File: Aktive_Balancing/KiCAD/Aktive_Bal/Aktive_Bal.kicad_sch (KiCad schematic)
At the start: 167 parts, among them J1 Conn_01x01_Pin, J2 Sockel_BluePill, J3 A-DF_09_A_KG-T4S, J4 Screw_Terminal_01x02, J5 Conn_01x01_Pin, J6 Conn_01x01_Pin, Q1 BSS316NH6327XTSA1, Q10 NTTFS6H888NL, Q11 NTTFS6H888NL, Q12 NTTFS6H888NL, Q13 NTTFS6H888NL, Q14 NTTFS6H888NL, Q15 NTTFS6H888NL, Q16 NTTFS6H888NL, Q17 NTTFS6H888NL, Q18 NTTFS6H888NL, Q19 NTTFS6H888NL, Q20 NTTFS6H888NL, Q21 NTTFS6H888NL, Q22 NTTFS6H888NL, Q23 NTTFS6H888NL, Q24 NTTFS6H888NL, Q25 NTTFS6H888NL, Q26 NTTFS6H888NL, Q27 NTTFS6H888NL, Q28 NTTFS6H888NL, Q29 NTTFS6H888NL, Q3 NTTFS6H888NL, Q30 NTTFS6H888NL, Q31 NTTFS6H888NL, Q32 NTTFS6H888NL, Q33 NTTFS6H888NL, Q34 NTTFS6H888NL, Q4 NTTFS6H888NL, Q5 NTTFS6H888NL, Q6 NTTFS6H888NL, Q7 NTTFS6H888NL, Q8 NTTFS6H888NL, Q9 NTTFS6H888NL, U1 SCW20C-12, U10 LTV-847S, U11 LTV-847S, U12 LTV-847S, U13 RFP12N10L, U14 PCF8575CDB, U15 SN65HVD233, U2 EC1SA16N, U3 LM2596S-ADJ, U4 TL084, U5 ADUM1250ARZ-RL7, U6 PCA9306DC, U7 LM1117IMPX_3_3_NOPB, U8 MCP4725xxx-xCH, U9 LTV-847S

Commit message: footprints zuggewiesen
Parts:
- C1: footprint (none) -> Capacitor_SMD:C_Elec_8x10.2
- C4: footprint (none) -> Capacitor_SMD:CP_Elec_5x5.3
- D1: footprint (none) -> Diode_SMD:D_SMA
- J4: footprint (none) -> TerminalBlock_MetzConnect:TerminalBlock_MetzConnect_Type055_RT01502HDWU_1x02_P5.00mm_Horizontal
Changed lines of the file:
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@@
 			)
 		)
-		(property "Footprint" ""
+		(property "Footprint" "TerminalBlock_MetzConnect:TerminalBlock_MetzConnect_Type055_RT01502HDWU_1x02_P5.00mm_Horizontal"
 			(at 24.13 40.64 0)
 			(hide yes)
@@
 			)
 		)
-		(property "Footprint" ""
+		(property "Footprint" "Capacitor_SMD:C_Elec_8x10.2"
 			(at 166.37 205.74 0)
 			(hide yes)
@@
 			)
 		)
-		(property "Footprint" ""
+		(property "Footprint" "Diode_SMD:D_SMA"
 			(at 200.025 214.63 0)
 			(hide yes)
@@
 			)
 		)
-		(property "Footprint" ""
+		(property "Footprint" "Capacitor_SMD:CP_Elec_5x5.3"
 			(at 216.8652 218.44 0)
 			(hide yes)

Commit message: footprints
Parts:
- added J7, J8, J9: Conn_01x01_Pin, Connector_PinHeader_2.54mm:PinHeader_1x01_P2.54mm_Vertical, symbol Connector:Conn_01x01_Pin
- J1, J5, J6: footprint (none) -> Connector_PinHeader_2.54mm:PinHeader_1x01_P2.54mm_Vertical
- JP1: footprint (none) -> Jumper:SolderJumper-2_P1.3mm_Bridged_Pad1.0x1.5mm
- JP2, JP3, JP4, JP5: footprint (none) -> Jumper:SolderJumper-2_P1.3mm_Open_TrianglePad1.0x1.5mm
- L1: footprint (none) -> Inductor_SMD:L_Bourns_SRR1260
- U10, U11, U12, U9: footprint LTV-847S:SOIC254P1016X460-16N -> Aktive_Bal_Footprints:SOIC254P1016X460-16N
- U13: footprint (none) -> Aktive_Bal_Footprints:TO-220AB_ONS
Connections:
- net +3.3V: now also J9.1 (Pin_1)
- net +5V: now also J7.1 (Pin_1)
- net -5V: now also J8.1 (Pin_1)
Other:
- moved on the sheet: C7, C8, U7

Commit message: kicad
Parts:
- C12: value 100n -> 0.1µ
- R37, R38, R39, R40, R41, R42, R43, R44, R45, R46, R47, R48, R49, R50, R51, R52: value 10k -> 100k
- R55, R57, R58, R59, R60, R61, R62, R63, R64, R65, R66, R67, R68, R69, R70, R71: value 100 -> 330
- R56, R72, R73, R74, R75, R76, R77, R78, R79, R80, R81, R82, R83, R84, R85, R86: value 1Meg -> 10Meg
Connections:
- net +5V: now also R21.1, R22.1, R23.1, R24.1, R25.1, R26.1, R27.1, R28.1, R29.1, R30.1, R31.1, R32.1, R33.1, R34.1, R35.1, R36.1
- net B1: now also U9.2; no longer R21.1
- net B10: now also U11.4; no longer R30.1
- net B11: now also U11.6; no longer R31.1
- net B12: now also U11.8; no longer R32.1
- net B13: now also U12.2; no longer R33.1
- net B14: now also U12.4; no longer R34.1
- net B15: now also U12.6; no longer R35.1
- net B16: now also U12.8; no longer R36.1
- net B2: now also U9.4; no longer R22.1
- net B3: now also U9.6; no longer R23.1
- net B4: now also U9.8; no longer R24.1
- net B5: now also U10.2; no longer R25.1
- net B6: now also U10.4; no longer R26.1
- net B7: now also U10.6; no longer R27.1
- net B8: now also U10.8; no longer R28.1
- net B9: now also U11.2; no longer R29.1
- net C0: no longer R56.2
- net GND_float2: now also R56.2; no longer U10.2, U10.4, U10.6, U10.8, U11.2, U11.4, U11.6, U11.8, U12.2, U12.4, U12.6, U12.8, U9.2, U9.4, U9.6, U9.8
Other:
- note added: "RG RGS"
- note added: "gndflota"
- moved on the sheet: R56

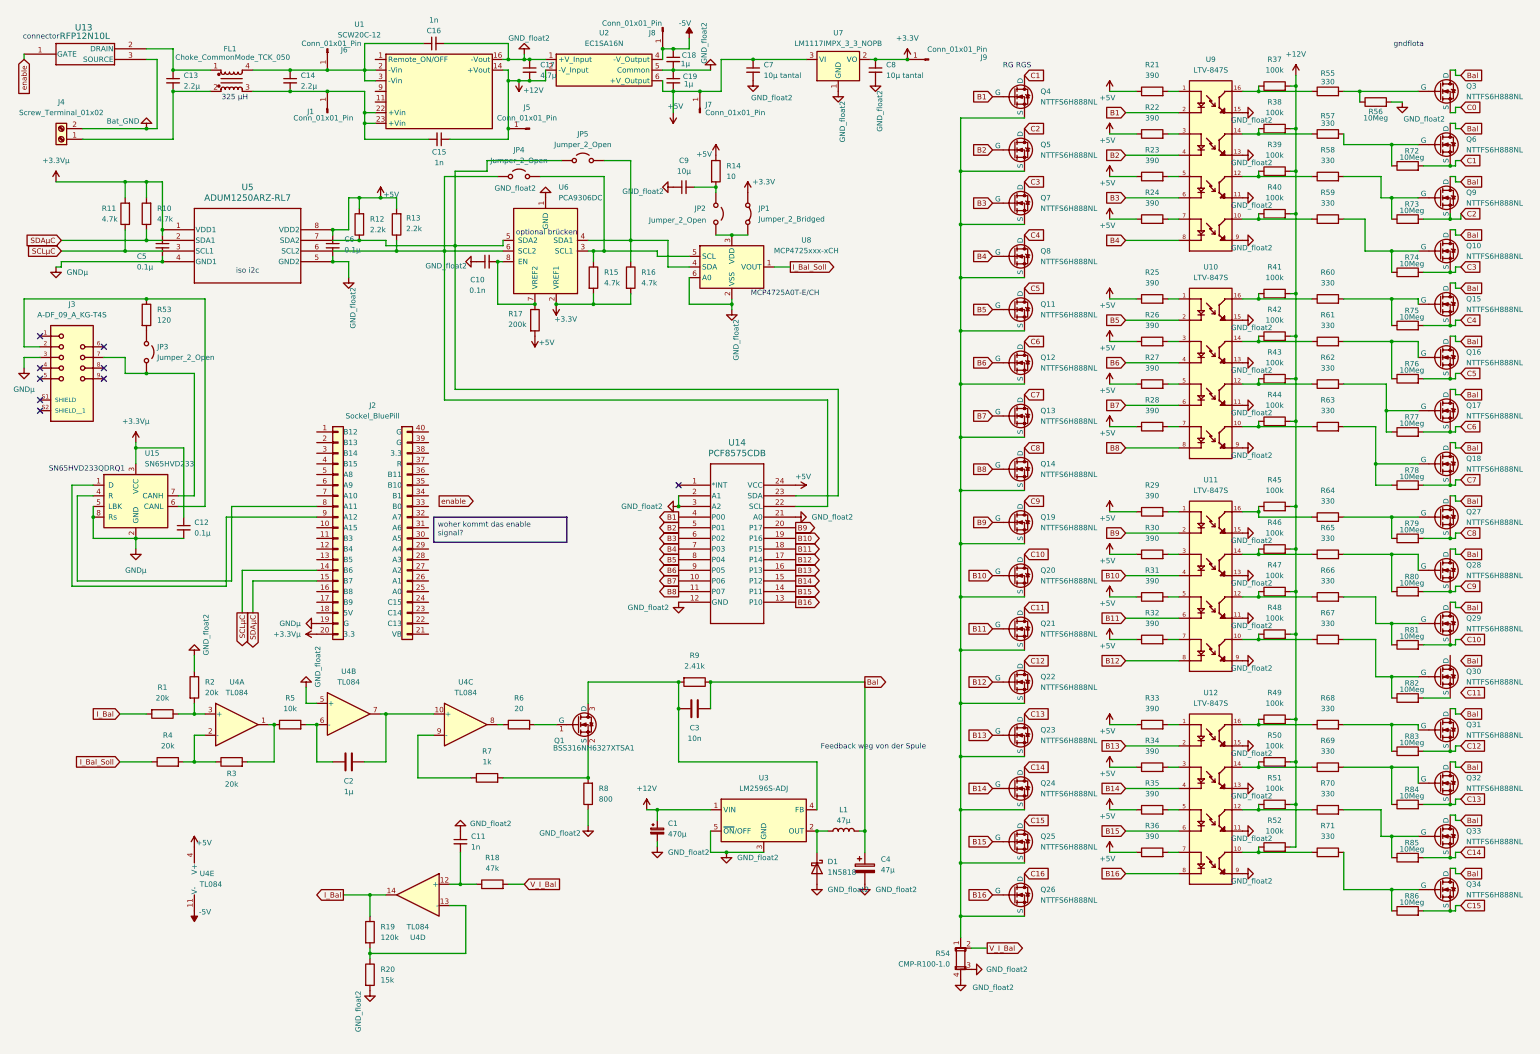
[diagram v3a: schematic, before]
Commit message: kicad sub strukturen
Den schaltplan in kleinere aufgeteilt
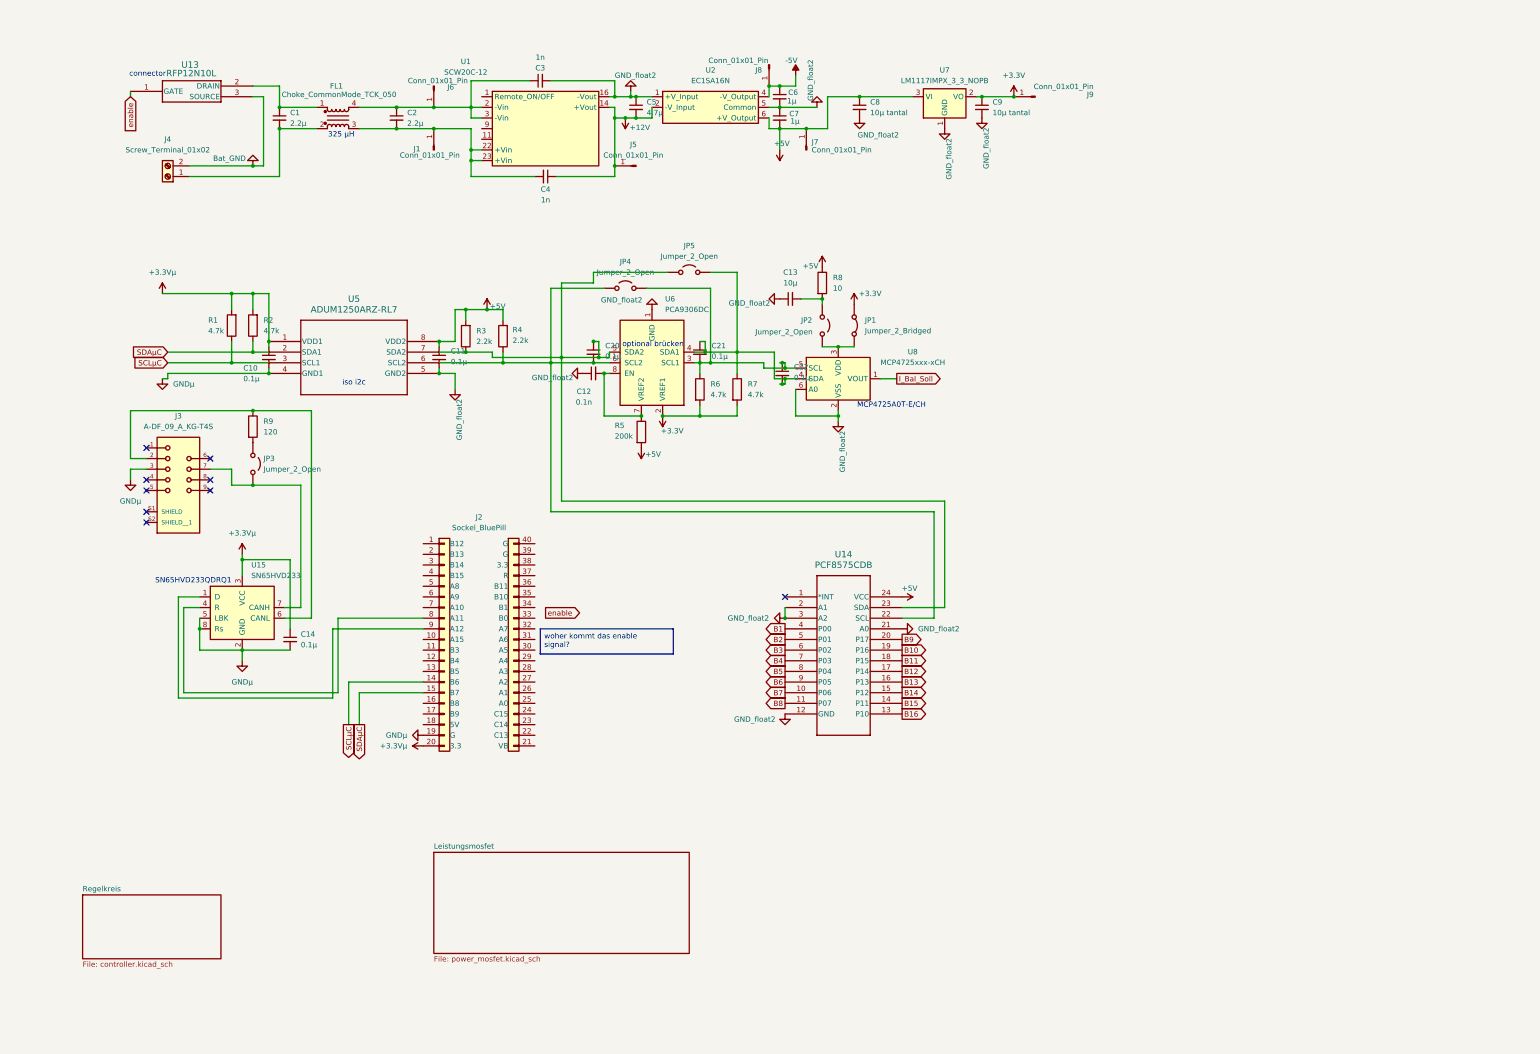
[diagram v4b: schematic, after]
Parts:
- removed C1: 470µ, Capacitor_SMD:C_Elec_8x10.2, symbol Device:C_Polarized_Small
- removed C11: 1n, Capacitor_SMD:C_0805_2012Metric, symbol Device:C_Small
- removed C2: 1µ, Capacitor_SMD:C_0805_2012Metric, symbol Device:C
- removed C3: 10n, Capacitor_SMD:C_0805_2012Metric, symbol Device:C
- removed C4: 47µ, Capacitor_SMD:CP_Elec_5x5.3, symbol Device:C_Polarized
- removed D1: 1N5818, Diode_SMD:D_SMA, symbol Diode:1N5818
- removed L1: 47µ, Inductor_SMD:L_Bourns_SRR1260, symbol Device:L
- removed Q1: BSS316NH6327XTSA1, Package_TO_SOT_SMD:SOT-23, symbol Aktive_Bal_Lib:BSS316NH6327XTSA1
- removed Q10, Q11, Q12, Q13, Q14, Q15, Q16, Q17, Q18, Q19, Q20, Q21, Q22, Q23, Q24, Q25, Q26, Q27, Q28, Q29, Q3, Q30, Q31, Q32, Q33, Q34, Q4, Q5, Q6, Q7, Q8, Q9: NTTFS6H888NL, Aktive_Bal_Footprints:8-WDFN, symbol Aktive_Bal_Lib:NTTFS6H888NL
- removed R1, R2, R3, R4: 20k, Resistor_SMD:R_0805_2012Metric, symbol Device:R
- removed R18: 47k, Resistor_SMD:R_0805_2012Metric, symbol Device:R
- removed R19: 120k, Resistor_SMD:R_0805_2012Metric, symbol Device:R
- removed R20: 15k, Resistor_SMD:R_0805_2012Metric, symbol Device:R
- removed R21, R22, R23, R24, R25, R26, R27, R28, R29, R30, R31, R32, R33, R34, R35, R36: 390, Resistor_SMD:R_0805_2012Metric, symbol Device:R
- removed R37, R38, R39, R40, R41, R42, R43, R44, R45, R46, R47, R48, R49, R50, R51, R52: 100k, Resistor_SMD:R_0805_2012Metric, symbol Device:R
- removed R5: 10k, Resistor_SMD:R_0805_2012Metric, symbol Device:R
- removed R54: CMP-R100-1.0, Aktive_Bal_Footprints:CMP-R100-1.0, symbol Aktive_Bal_Lib:CMP-R100-1.0
- removed R55, R57, R58, R59, R60, R61, R62, R63, R64, R65, R66, R67, R68, R69, R70, R71: 330, Resistor_SMD:R_0805_2012Metric, symbol Device:R
- removed R56, R72, R73, R74, R75, R76, R77, R78, R79, R80, R81, R82, R83, R84, R85, R86: 10Meg, Resistor_SMD:R_0805_2012Metric, symbol Device:R
- removed R6: 20, Resistor_SMD:R_0805_2012Metric, symbol Device:R
- removed R7: 1k, Resistor_SMD:R_0805_2012Metric, symbol Device:R
- removed R8: 800, Resistor_SMD:R_0805_2012Metric, symbol Device:R
- removed R9: 2.41k, Resistor_SMD:R_0805_2012Metric, symbol Device:R
- removed U10, U11, U12, U9: LTV-847S, Aktive_Bal_Footprints:SOIC254P1016X460-16N, symbol Aktive_Bal_Lib:LTV-847S
- removed U3: LM2596S-ADJ, Package_TO_SOT_SMD:TO-263-5_TabPin3, symbol Regulator_Switching:LM2596S-ADJ
- removed U4: TL084, Package_SO:SOIC-14_3.9x8.7mm_P1.27mm, symbol Amplifier_Operational:TL084
- added C20, C21, C22: 0.1µ, Capacitor_SMD:C_0805_2012Metric, symbol Device:C_Small
- renumbered C13 to C1, C5 to C10, C6 to C11, C10 to C12, C9 to C13, C12 to C14, C14 to C2, C16 to C3, C15 to C4, C17 to C5, C18 to C6, C19 to C7, C7 to C8, C8 to C9, R11 to R1, R10 to R2, R12 to R3, R13 to R4, R17 to R5, R15 to R6, R16 to R7, R14 to R8, R53 to R9
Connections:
- net at JP5.1 (A), R3.1, U14.23 (SDA)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: now also C20.1
- net at JP4.1 (A), R4.1, U14.22 (SCL)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: now also C20.2
- net at JP4.2 (B), R6.1, U6.3 (SCL1)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: now also C21.2, C22.1
- net at JP5.2 (B), R7.1, U6.4 (SDA1)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: now also C21.1, C22.2
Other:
- added sheet Leistungsmosfet (power_mosfet.kicad_sch)
- added sheet Regelkreis (controller.kicad_sch)
- note removed: "Feedback weg von der Spule"
- note removed: "RG RGS"
- note removed: "gndflota"
- moved on the sheet: C1, C10, C11, C12, C13, C14, C2, C3, C4, C5, C6, C7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

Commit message: kicad
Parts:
- removed C22: 0.1µ, Capacitor_SMD:C_0805_2012Metric, symbol Device:C_Small
- removed J1, J5, J6, J7, J8: Conn_01x01_Pin, Connector_PinHeader_2.54mm:PinHeader_1x01_P2.54mm_Vertical, symbol Connector:Conn_01x01_Pin
- removed JP1: Jumper_2_Bridged, Jumper:SolderJumper-2_P1.3mm_Bridged_Pad1.0x1.5mm, symbol Jumper:Jumper_2_Bridged
- removed JP2: Jumper_2_Open, Jumper:SolderJumper-2_P1.3mm_Open_TrianglePad1.0x1.5mm, symbol Jumper:Jumper_2_Open
- added C23: 0.1µ, symbol Device:C
- added C25, C26, C27, C28: 0.1µ, Capacitor_SMD:C_0805_2012Metric, symbol Device:C_Small
- added C29: 1n, Capacitor_SMD:C_0805_2012Metric, symbol Device:C_Small
- added J16, J17, J18, J19, J20, J21: Conn_01x02_Pin, symbol Connector:Conn_01x02_Pin
- added JP6: Jumper_3_Bridged12, symbol Jumper:Jumper_3_Bridged12
- added R25: 1Meg, Resistor_SMD:R_0805_2012Metric, symbol Device:R
- C20: value 0.1µ -> 10µ
- C6, C7: value 1µ -> 10µ
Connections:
- net +12V: now also J17.1 (Pin_1)
- net +3.3V: now also JP6.3 (B)
- net +3.3Vµ: now also C14.2, C23.1; no longer C14.1
- net +5V: now also C26.2, C28.2, J18.1 (Pin_1)
- net -5V: now also C25.1, J18.2 (Pin_2)
- net GND_float2: now also C20.1, C25.2, C26.1, C27.1, C28.1, J17.2 (Pin_2)
- net GNDµ: now also C14.1, C23.2, C29.1, R25.1; no longer C14.2
- net SCLµC: now also J21.2 (Pin_2)
- net SDAµC: now also J21.1 (Pin_1)
- net at JP5.1 (A), R3.1, U14.23 (SDA)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: now also J19.1 (Pin_1); no longer C20.1
- net at JP4.1 (A), R4.1, U14.22 (SCL)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: now also J19.2 (Pin_2); no longer C20.2
- net at U8.3 (VDD): now also C20.2, C27.2, JP6.2 (C)
- net at C21.2, JP4.2 (B), R6.1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: now also J20.2 (Pin_2)
- net at C2.2, C4.2, FL1.3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: now also J16.2 (Pin_2)
- net at C2.1, C3.1, FL1.4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: now also J16.1 (Pin_1)
- net at C13.2, R8.2: now also JP6.1 (A)
- net at C21.1, JP5.2 (B), R7.1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: now also J20.1 (Pin_1)
- net at J3.5: now also J3.S1 (SHIELD), J3.S2 (SHIELD__1), C29.2, R25.2
- no-connect marks 9 -> 6
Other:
- note removed: "optional brücken"
- moved on the sheet: C13, C14, C21, C5, C6, C7, C8, C9, J9, R8, U2, U7

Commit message: kicad
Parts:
- added C30: 0.1µ, Capacitor_SMD:C_0805_2012Metric, symbol Device:C_Small
- added C32, C33: 0.1µ, symbol Device:C
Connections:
- net +3.3V: now also C21.2, C33.2
- net +5V: now also C32.2
- net GND_float2: now also C21.1, C30.1, C32.1, C33.1
- net at C12.2, R5.1, U6.7 (VREF2)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: now also C30.2
- net at J20.2 (Pin_2), JP4.2 (B), R6.1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: no longer C21.2
- net at J20.1 (Pin_1), JP5.2 (B), R7.1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: no longer C21.1
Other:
- moved on the sheet: R5

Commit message: kicad bom
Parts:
- renumbered C8 to C10, C32 to C11, C9 to C12, C33 to C13, C10 to C14, C11 to C15, C12 to C16, C21 to C18, C30 to C19, C27 to C20, C20 to C21, C13 to C22, C29 to C23, C14 to C24, C23 to C25, C28 to C26, C25 to C8, C26 to C9
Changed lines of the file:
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@@
 	(generator_version "10.0")
 	(paper "A3")
+	(bezier
+		(pts
+			(xy 54.864 213.868) (xy 54.864 213.868) (xy 54.864 213.868) (xy 54.864 213.868)
+		)
+		(stroke
+			(width 0)
+			(type default)
+		)
+		(fill
+			(type none)
+		)
+	)
 	(text "connector \n"
 		(exclude_from_sim no)
@@
 		(in_pos_files yes)
 		(dnp no)
-		(property "Reference" "C11"
+		(property "Reference" "C15"
 			(at 112.776 84.328 0)
 			(show_name no)
@@
 			(project "Aktive_Bal"
 				(path "/7c40c112-cd2b-4a48-9744-14a65613b3b5"
-					(reference "C11")
+					(reference "C15")
 					(unit 1)
 				)
@@
 		(in_pos_files yes)
 		(dnp no)
-		(property "Reference" "C12"
+		(property "Reference" "C16"
 			(at 148.844 100.838 90)
 			(show_name no)
@@
 			(project "Aktive_Bal"
 				(path "/7c40c112-cd2b-4a48-9744-14a65613b3b5"
-					(reference "C12")
+					(reference "C16")
 					(unit 1)
 				)
@@
 		(in_pos_files yes)
 		(dnp no)
-		(property "Reference" "C25"
+		(property "Reference" "C8"
 			(at 214.122 29.464 0)
 			(show_name no)
@@
 			(project "Aktive_Bal"
 				(path "/7c40c112-cd2b-4a48-9744-14a65613b3b5"
-					(reference "C25")
+					(reference "C8")
 					(unit 1)
 				)
@@
 		(dnp no)
 		(fields_autoplaced yes)
-		(property "Reference" "C13"
+		(property "Reference" "C22"
 			(at 198.1263 55.88 90)
 			(show_name no)
@@
 			(project "Aktive_Bal"
 				(path "/7c40c112-cd2b-4a48-9744-14a65613b3b5"
-					(reference "C13")
+					(reference "C22")
 					(unit 1)
 				)
@@
 		(in_pos_files yes)
 		(dnp no)
-		(property "Reference" "C10"
+		(property "Reference" "C14"
 			(at 67.564 95.25 0)
 			(show_name no)
@@
 			(project "Aktive_Bal"
 				(path "/7c40c112-cd2b-4a48-9744-14a65613b3b5"
-					(reference "C10")
+					(reference "C14")
 					(unit 1)
 				)
@@
 		(in_pos_files yes)
 		(dnp no)
-		(property "Reference" "C27"
+		(property "Reference" "C20"
 			(at 214.884 85.852 90)
 			(show_name no)
@@
 			(project "Aktive_Bal"
 				(path "/7c40c112-cd2b-4a48-9744-14a65613b3b5"
-					(reference "C27")
+					(reference "C20")
 					(unit 1)
 				)
@@
 		(in_pos_files yes)
 		(dnp no)
-		(property "Reference" "C28"
+		(property "Reference" "C26"
 			(at 220.726 145.034 0)
 			(show_name no)
@@
 			(project "Aktive_Bal"
 				(path "/7c40c112-cd2b-4a48-9744-14a65613b3b5"
-					(reference "C28")
+					(reference "C26")
 					(unit 1)
 				)
@@
 		(in_pos_files yes)
 		(dnp no)
-		(property "Reference" "C21"
+		(property "Reference" "C18"
 			(at 175.514 109.728 90)
 			(show_name no)
@@
 			(project "Aktive_Bal"
 				(path "/7c40c112-cd2b-4a48-9744-14a65613b3b5"
-					(reference "C21")
+					(reference "C18")
 					(unit 1)
 				)
@@
 		(dnp no)
 		(fields_autoplaced yes)
-		(property "Reference" "C23"
+		(property "Reference" "C25"
 			(at 114.3 187.9599 0)
 			(show_name no)
@@
 			(project "Aktive_Bal"
 				(path "/7c40c112-cd2b-4a48-9744-14a65613b3b5"
-					(reference "C23")
+					(reference "C25")
 					(unit 1)
 				)
@@
 		(in_pos_files yes)
 		(dnp no)
-		(property "Reference" "C29"
+		(property "Reference" "C23"
 			(at 32.766 126.238 90)
 			(show_name no)
@@
 			(project "Aktive_Bal"
 				(path "/7c40c112-cd2b-4a48-9744-14a65613b3b5"
-					(reference "C29")
+					(reference "C23")
 					(unit 1)
 				)
@@
 		(in_pos_files yes)
 		(dnp no)
-		(property "Reference" "C26"
+		(property "Reference" "C9"
 			(at 214.0973 34.544 0)
 			(show_name no)
@@
 			(project "Aktive_Bal"
 				(path "/7c40c112-cd2b-4a48-9744-14a65613b3b5"
-					(reference "C26")
+					(reference "C9")
 					(unit 1)
 				)
@@
 		(in_pos_files yes)
 		(dnp no)
-		(property "Reference" "C20"
+		(property "Reference" "C21"
 			(at 214.63 80.772 90)
 			(show_name no)
@@
 			(project "Aktive_Bal"
 				(path "/7c40c112-cd2b-4a48-9744-14a65613b3b5"
-					(reference "C20")
+					(reference "C21")
 					(unit 1)
 				)
@@
 		(dnp no)
 		(fields_autoplaced yes)
-		(property "Reference" "C33"
+		(property "Reference" "C13"
 			(at 269.24 15.24 90)
 			(show_name no)
@@
 			(project "Aktive_Bal"
 				(path "/7c40c112-cd2b-4a48-9744-14a65613b3b5"
-					(reference "C33")
+					(reference "C13")
 					(unit 1)
 				)
@@
 		(in_pos_files yes)
 		(dnp no)
-		(property "Reference" "C30"
+		(property "Reference" "C19"
 			(at 164.338 116.8335 0)
 			(show_name no)
@@
 			(project "Aktive_Bal"
 				(path "/7c40c112-cd2b-4a48-9744-14a65613b3b5"
-					(reference "C30")
+					(reference "C19")
 					(unit 1)
 				)
@@
 		(dnp no)
 		(fields_autoplaced yes)
-		(property "Reference" "C32"
+		(property "Reference" "C11"
 			(at 248.92 22.86 90)
 			(show_name no)
@@
 			(project "Aktive_Bal"
 				(path "/7c40c112-cd2b-4a48-9744-14a65613b3b5"
-					(reference "C32")
+					(reference "C11")
 					(unit 1)
 				)
@@
 		(dnp no)
 		(fields_autoplaced yes)
-		(property "Reference" "C8"
+		(property "Reference" "C10"
 			(at 243.84 39.3762 0)
 			(show_name no)
@@
 			(project "Aktive_Bal"
 				(path "/7c40c112-cd2b-4a48-9744-14a65613b3b5"
-					(reference "C8")
+					(reference "C10")
 					(unit 1)
 				)
@@
 		(in_pos_files yes)
 		(dnp no)
-		(property "Reference" "C14"
+		(property "Reference" "C24"
 			(at 59.436 136.398 90)
 			(show_name no)
@@
 			(project "Aktive_Bal"
 				(path "/7c40c112-cd2b-4a48-9744-14a65613b3b5"
-					(reference "C14")
+					(reference "C24")
 					(unit 1)
 				)
@@
 		(dnp no)
 		(fields_autoplaced yes)
-		(property "Reference" "C9"
+		(property "Reference" "C12"
 			(at 273.05 39.3762 0)
 			(show_name no)
@@
 			(project "Aktive_Bal"
 				(path "/7c40c112-cd2b-4a48-9744-14a65613b3b5"
-					(reference "C9")
+					(reference "C12")
 					(unit 1)
 				)
